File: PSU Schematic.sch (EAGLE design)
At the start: 19 parts, among them IC1 LM34, J1 POWERPOLE_POWER45A, J2 FUSEATC, J3 POWERPOLE_POWER45A, J4 FUSEATC

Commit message: Layout revision
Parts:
- renumbered U$2 to CS
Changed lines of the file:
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@@
 <part name="R4" library="pot" deviceset="TRIM_EU-" device="RJ9W" value="T93YA"/>
 <part name="GND5" library="supply1" deviceset="GND" device=""/>
-<part name="U$2" library="con-lstb" deviceset="SINGLE" device=""/>
+<part name="CS" library="con-lstb" deviceset="SINGLE" device=""/>
 <part name="R3" library="pot" deviceset="TRIM_EU-" device="RJ9W" value="T93YA"/>
 </parts>
@@
 <instance part="R4" gate="1" x="109.22" y="58.42" rot="R180"/>
 <instance part="GND5" gate="1" x="99.06" y="-12.7" rot="R270"/>
-<instance part="U$2" gate="G$1" x="86.36" y="35.56" rot="R180"/>
+<instance part="CS" gate="G$1" x="86.36" y="35.56" rot="R180"/>
 <instance part="R3" gate="1" x="109.22" y="-17.78" rot="R180"/>
 </instances>
@@
 <segment>
 <pinref part="U$1" gate="G$1" pin="SIG11"/>
-<pinref part="U$2" gate="G$1" pin="3"/>
+<pinref part="CS" gate="G$1" pin="3"/>
 <wire x1="63.5" y1="33.02" x2="78.74" y2="33.02" width="0.1524" layer="91"/>
 </segment>

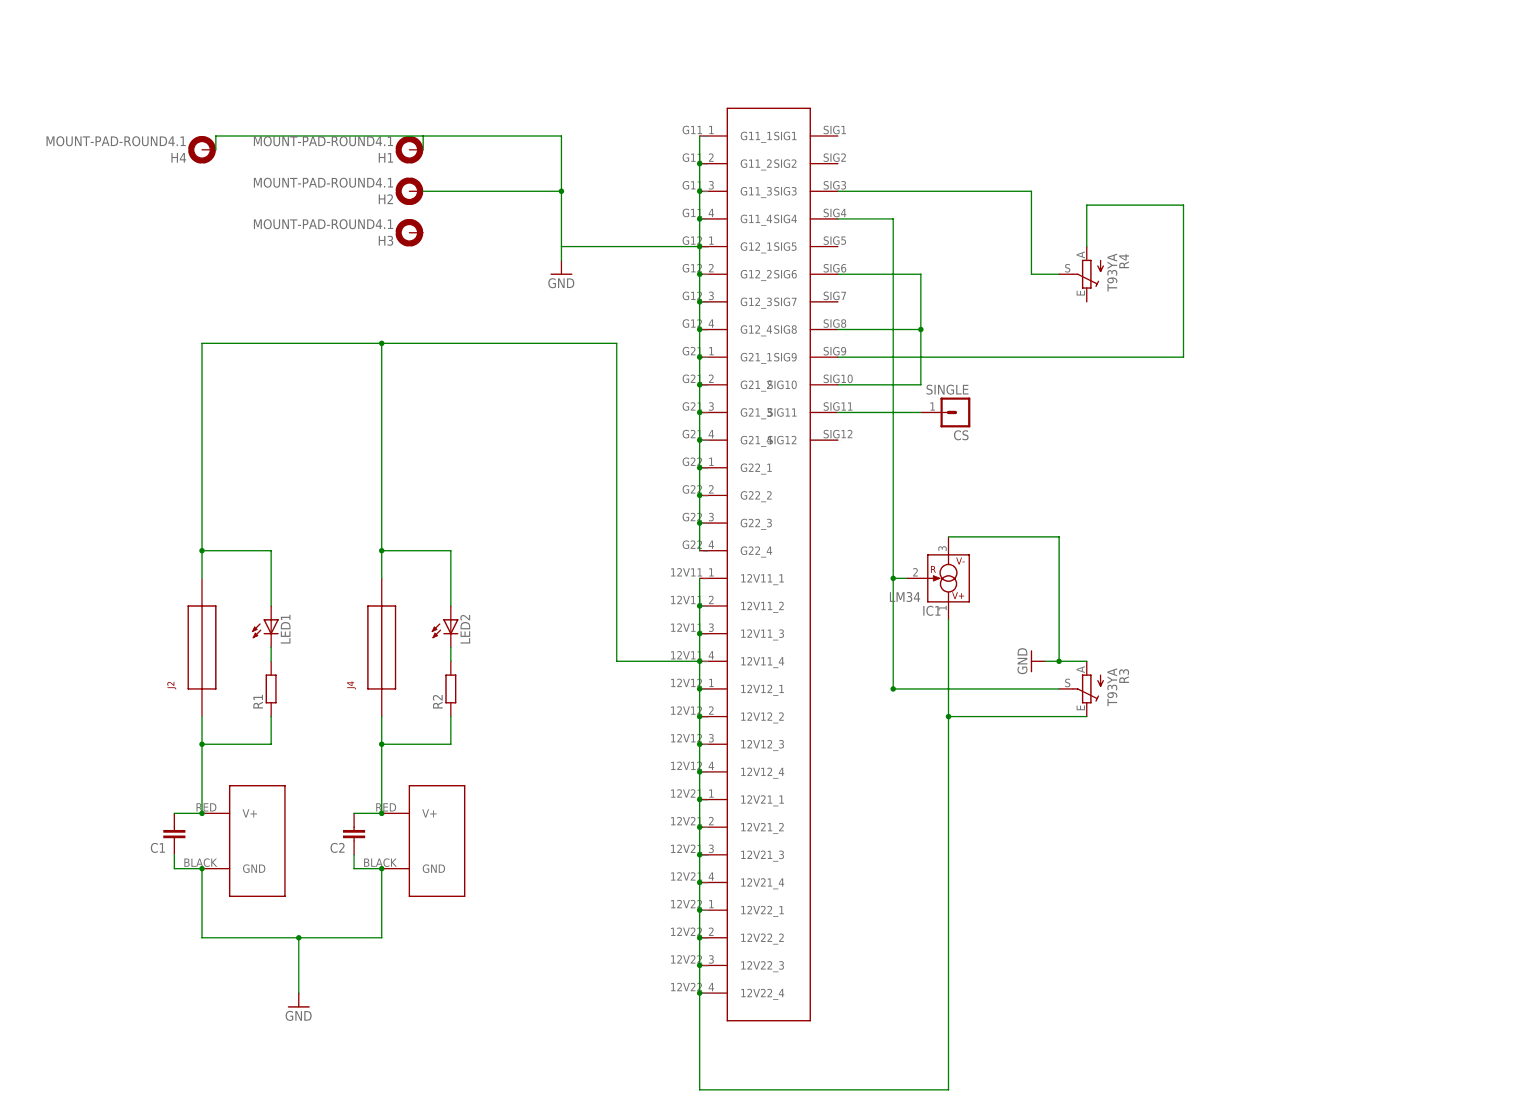
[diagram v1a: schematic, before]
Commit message: Corrected layout
Flipped design to correct mis-match which would have occured.
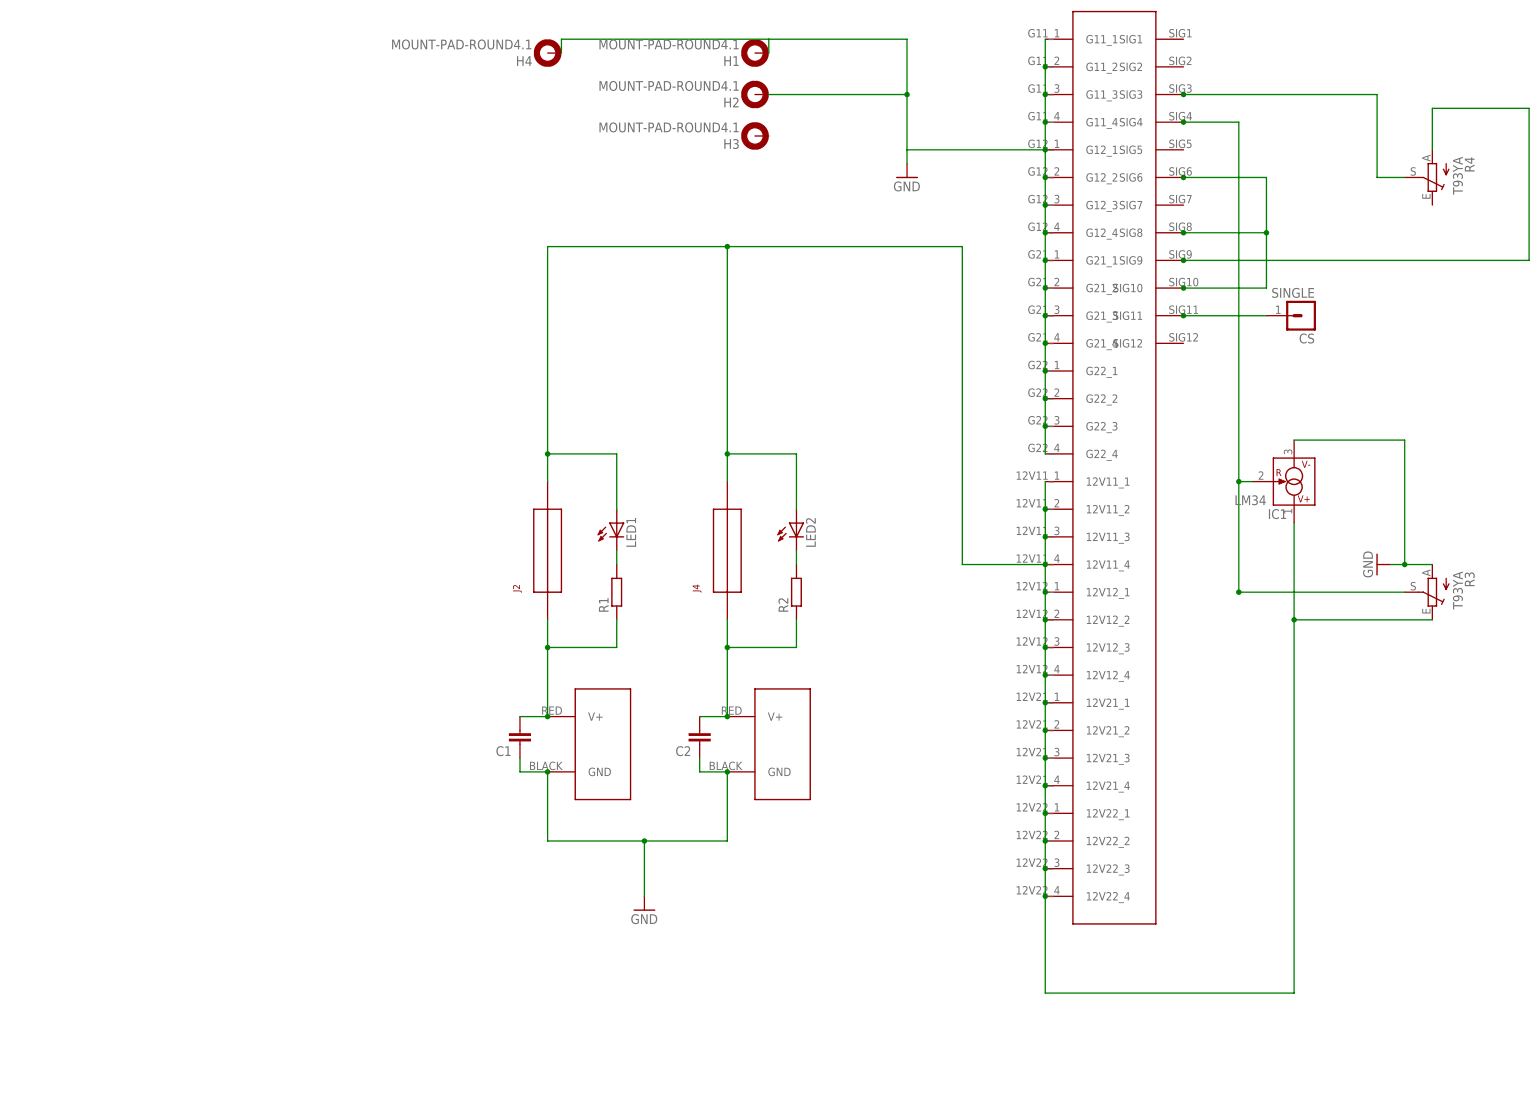
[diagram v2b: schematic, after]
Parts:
- removed U$1: 51730-073LF, PowerEdge:51730-073LF
- added U$2: 51760-10201202AALF51760-10201202AALF, PowerEdge:51760-10201202AALF51760-10201202AALF
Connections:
- net 5VCC: now also U$2.SIG3; no longer U$1.SIG3
- net CURRENTSHARE: now also U$2.SIG11; no longer U$1.SIG11
- net FAN: now also U$2.SIG4; no longer U$1.SIG4
- net GND: now also U$2.G11_1, U$2.G11_2, U$2.G11_3, U$2.G11_4, U$2.G12_1, U$2.G12_2, U$2.G12_3, U$2.G12_4, U$2.G21_1, U$2.G21_2, U$2.G21_3, U$2.G21_4, U$2.G22_1, U$2.G22_2, U$2.G22_3, U$2.G22_4; no longer U$1.G11_1, U$1.G11_2, U$1.G11_3, U$1.G11_4, U$1.G12_1, U$1.G12_2, U$1.G12_3, U$1.G12_4, U$1.G21_1, U$1.G21_2, U$1.G21_3, U$1.G21_4, U$1.G22_1, U$1.G22_2, U$1.G22_3, U$1.G22_4
- net LVCC: now also U$2.12V11_1, U$2.12V11_2, U$2.12V11_3, U$2.12V11_4, U$2.12V12_1, U$2.12V12_2, U$2.12V12_3, U$2.12V12_4, U$2.12V21_1, U$2.12V21_2, U$2.12V21_3, U$2.12V21_4, U$2.12V22_1, U$2.12V22_2, U$2.12V22_3, U$2.12V22_4; no longer U$1.12V11_1, U$1.12V11_2, U$1.12V11_3, U$1.12V11_4, U$1.12V12_1, U$1.12V12_2, U$1.12V12_3, U$1.12V12_4, U$1.12V21_1, U$1.12V21_2, U$1.12V21_3, U$1.12V21_4, U$1.12V22_1, U$1.12V22_2, U$1.12V22_3, U$1.12V22_4
- net PSON: now also U$2.SIG10, U$2.SIG6, U$2.SIG8; no longer U$1.SIG10, U$1.SIG6, U$1.SIG8
- net VCTRL: now also U$2.SIG9; no longer U$1.SIG9
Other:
- moved on the sheet: C1, C2, CS, H1, H2, H3, H4, IC1, J2, J4, LED1, LED2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

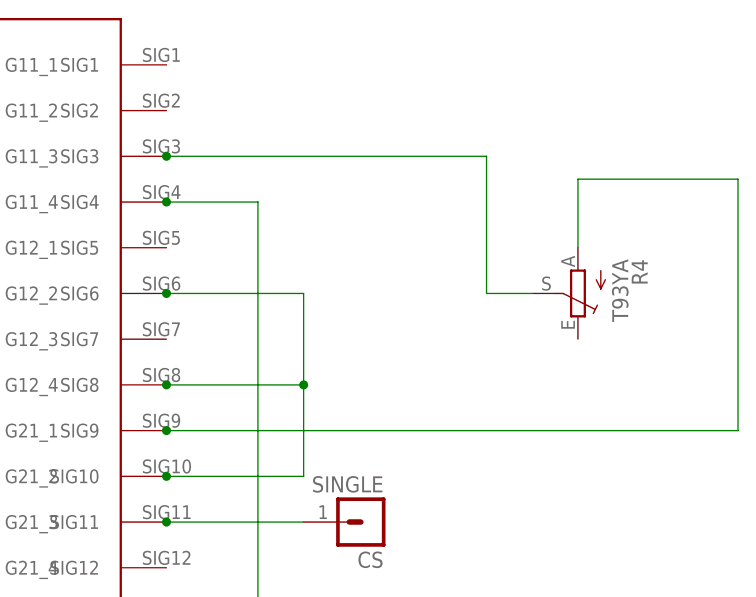
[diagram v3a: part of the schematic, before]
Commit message: Added voltage decrease. Design Rules Updated.
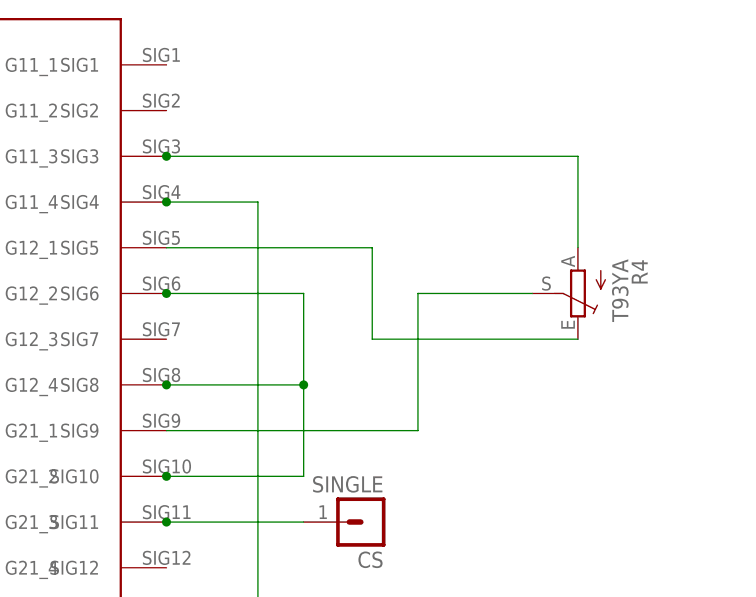
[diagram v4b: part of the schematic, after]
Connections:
- removed net VCTRL: R4.A, U$2.SIG9
- new net N$1: R4.E, U$2.SIG5
- new net N$2: R4.S, U$2.SIG9
- net 5VCC: now also R4.A; no longer R4.S
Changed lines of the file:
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@@
 <net name="5VCC" class="0">
 <segment>
-<pinref part="R4" gate="1" pin="S"/>
-<wire x1="127" y1="91.44" x2="162.56" y2="91.44" width="0.1524" layer="91"/>
-<wire x1="167.64" y1="76.2" x2="162.56" y2="76.2" width="0.1524" layer="91"/>
-<wire x1="162.56" y1="76.2" x2="162.56" y2="91.44" width="0.1524" layer="91"/>
+<wire x1="127" y1="91.44" x2="172.72" y2="91.44" width="0.1524" layer="91"/>
 <pinref part="U$2" gate="G$1" pin="SIG3"/>
 <junction x="127" y="91.44"/>
-</segment>
-</net>
-<net name="VCTRL" class="0">
-<segment>
-<wire x1="190.5" y1="60.96" x2="127" y2="60.96" width="0.1524" layer="91"/>
-<wire x1="190.5" y1="60.96" x2="190.5" y2="88.9" width="0.1524" layer="91"/>
-<wire x1="190.5" y1="88.9" x2="172.72" y2="88.9" width="0.1524" layer="91"/>
 <pinref part="R4" gate="1" pin="A"/>
-<wire x1="172.72" y1="88.9" x2="172.72" y2="81.28" width="0.1524" layer="91"/>
-<pinref part="U$2" gate="G$1" pin="SIG9"/>
-<junction x="127" y="60.96"/>
+<wire x1="172.72" y1="91.44" x2="172.72" y2="81.28" width="0.1524" layer="91"/>
 </segment>
 </net>
@@
 </segment>
 </net>
+<net name="N$1" class="0">
+<segment>
+<pinref part="R4" gate="1" pin="E"/>
+<wire x1="172.72" y1="71.12" x2="149.86" y2="71.12" width="0.1524" layer="91"/>
+<wire x1="149.86" y1="71.12" x2="149.86" y2="81.28" width="0.1524" layer="91"/>
+<pinref part="U$2" gate="G$1" pin="SIG5"/>
+<wire x1="149.86" y1="81.28" x2="127" y2="81.28" width="0.1524" layer="91"/>
+</segment>
+</net>
+<net name="N$2" class="0">
+<segment>
+<pinref part="R4" gate="1" pin="S"/>
+<wire x1="167.64" y1="76.2" x2="154.94" y2="76.2" width="0.1524" layer="91"/>
+<wire x1="154.94" y1="76.2" x2="154.94" y2="60.96" width="0.1524" layer="91"/>
+<pinref part="U$2" gate="G$1" pin="SIG9"/>
+<wire x1="154.94" y1="60.96" x2="127" y2="60.96" width="0.1524" layer="91"/>
+</segment>
+</net>
